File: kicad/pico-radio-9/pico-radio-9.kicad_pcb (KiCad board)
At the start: 2 copper layers, 115.8 x 67.5 mm, 58 parts, among them J1 FM antenna, J2 SW antenna, J3 MW/SW antenna kapcsoló, J4 HF Amplifier, J5 Batterry, Q1 PN2222A, Q2 PN2222A, Q3 PN2222A, SW1 Reset, U1 SI4732-A10-GS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

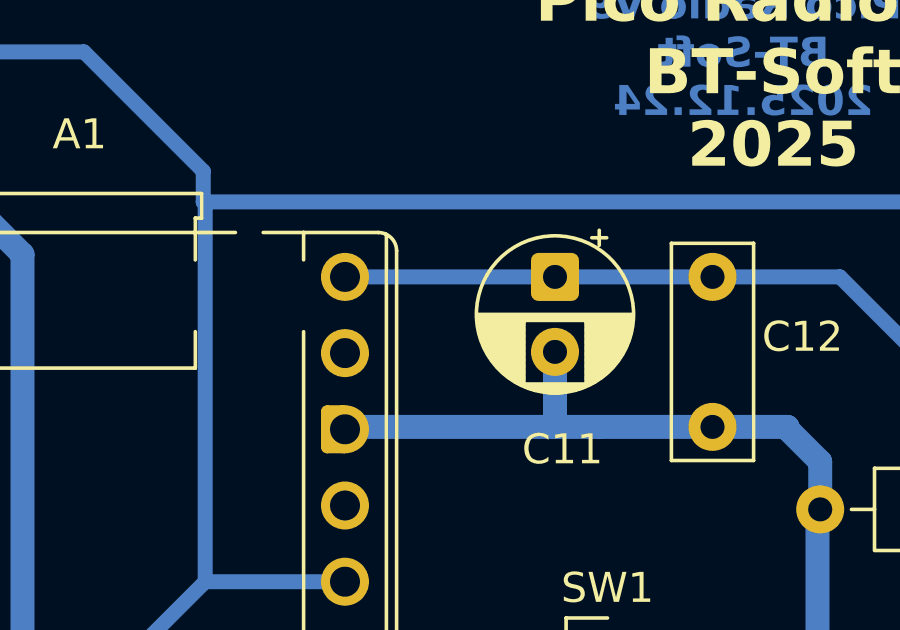
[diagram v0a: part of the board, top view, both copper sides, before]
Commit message: Vsys - Vbus power modification
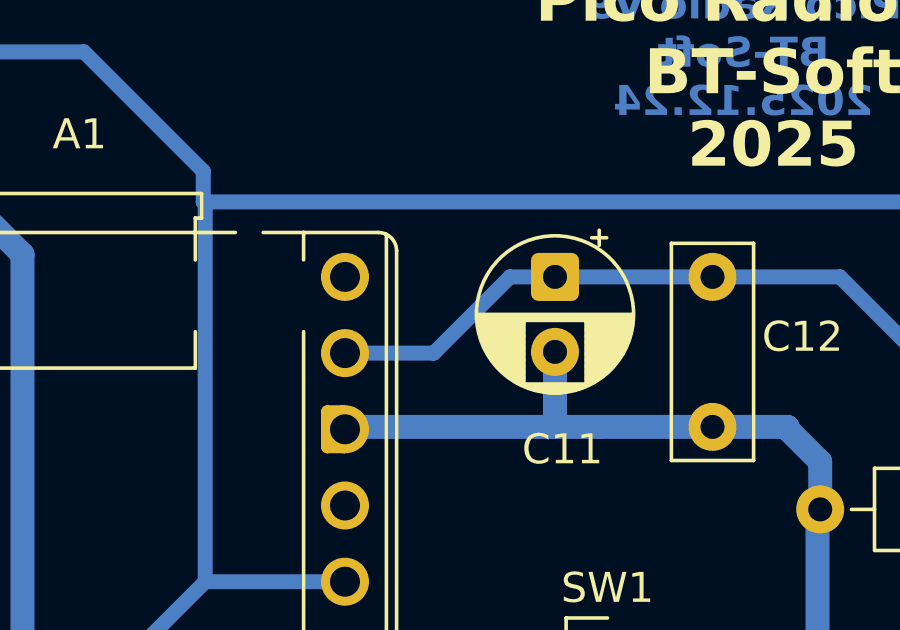
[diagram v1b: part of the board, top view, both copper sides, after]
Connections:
- A1 pad 40: +Vbus -> unconnected-(A1-VBUS-Pad40)
- BZ1 pad 1: +Vbus -> +Vsys
- C11 pad 1: +Vbus -> +Vsys
- C12 pad 1: +Vbus -> +Vsys
- JP4 pad 2: +Vbus -> +Vsys
- R12 pad 1: +Vbus -> +Vsys
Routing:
- net +Vsys: track 0.00 -> 59.6 mm
- net +Vbus: track 58.5 -> 0.00 mm
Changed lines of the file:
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@@
 	(net 16 "BUZZER")
 	(net 17 "/RST")
-	(net 18 "+Vbus")
+	(net 18 "unconnected-(A1-VBUS-Pad40)")
 	(net 19 "/SDI")
 	(net 20 "unconnected-(A1-GPIO23-Pad26)")
@@
 			(layers "*.Cu" "*.Mask")
 			(remove_unused_layers no)
-			(net 18 "+Vbus")
+			(net 4 "+Vsys")
 			(pinfunction "+")
 			(pintype "passive")
@@
 			(layers "*.Cu" "*.Mask")
 			(remove_unused_layers no)
-			(net 18 "+Vbus")
+			(net 18 "unconnected-(A1-VBUS-Pad40)")
 			(pinfunction "VBUS")
-			(pintype "power_out")
+			(pintype "power_out+no_connect")
 		)
 		(group ""
@@
 			(remove_unused_layers no)
 			(roundrect_rratio 0.15625)
-			(net 18 "+Vbus")
+			(net 4 "+Vsys")
 			(pintype "passive")
 		)
@@
 			(layers "*.Cu" "*.Mask")
 			(remove_unused_layers no)
-			(net 18 "+Vbus")
+			(net 4 "+Vsys")
 			(pintype "passive")
 		)
@@
 			(layers "*.Cu" "*.Mask")
 			(remove_unused_layers no)
-			(net 18 "+Vbus")
+			(net 4 "+Vsys")
 			(pinfunction "B")
 			(pintype "passive")
@@
 			(layers "*.Cu" "*.Mask")
 			(remove_unused_layers no)
-			(net 18 "+Vbus")
+			(net 4 "+Vsys")
 			(pintype "passive")
 		)
@@
 	)
 	(segment
+		(start 132.025 77.065)
+		(end 131.975 77.115)
+		(width 0.2)
+		(layer "B.Cu")
+		(net 4)
+	)
+	(segment
+		(start 132.025 69.275)
+		(end 132.025 77.065)
+		(width 0.5)
+		(layer "B.Cu")
+		(net 4)
+	)
+	(segment
+		(start 118.225 38.525)
+		(end 116.725 38.525)
+		(width 0.5)
+		(layer "B.Cu")
+		(net 4)
+	)
+	(segment
+		(start 116.725 38.525)
+		(end 114.185 41.065)
+		(width 0.5)
+		(layer "B.Cu")
+		(net 4)
+	)
+	(segment
+		(start 123.475 38.525)
+		(end 127.725 38.525)
+		(width 0.5)
+		(layer "B.Cu")
+		(net 4)
+	)
+	(segment
+		(start 131.725 51.195)
+		(end 131.725 55.525)
+		(width 0.5)
+		(layer "B.Cu")
+		(net 4)
+	)
+	(segment
+		(start 134.475 58.275)
+		(end 134.475 64.025)
+		(width 0.5)
+		(layer "B.Cu")
+		(net 4)
+	)
+	(segment
+		(start 118.225 38.525)
+		(end 123.475 38.525)
+		(width 0.5)
+		(layer "B.Cu")
+		(net 4)
+	)
+	(segment
+		(start 131.975 69.325)
+		(end 132.025 69.275)
+		(width 0.2)
+		(layer "B.Cu")
+		(net 4)
+	)
+	(segment
+		(start 132.025 66.475)
+		(end 132.025 68.724)
+		(width 0.5)
+		(layer "B.Cu")
+		(net 4)
+	)
+	(segment
+		(start 131.725 55.525)
+		(end 134.475 58.275)
+		(width 0.5)
+		(layer "B.Cu")
+		(net 4)
+	)
+	(segment
+		(start 114.185 41.065)
+		(end 111.225 41.065)
+		(width 0.5)
+		(layer "B.Cu")
+		(net 4)
+	)
+	(segment
+		(start 134.475 64.025)
+		(end 132.025 66.475)
+		(width 0.5)
+		(layer "B.Cu")
+		(net 4)
+	)
+	(segment
+		(start 131.725 42.525)
+		(end 131.725 51.195)
+		(width 0.5)
+		(layer "B.Cu")
+		(net 4)
+	)
+	(segment
+		(start 131.975 69.876)
+		(end 132.025 69.826)
+		(width 0.2)
+		(layer "B.Cu")
+		(net 4)
+	)
+	(segment
+		(start 127.725 38.525)
+		(end 131.725 42.525)
+		(width 0.5)
+		(layer "B.Cu")
+		(net 4)
+	)
+	(segment
 		(start 93.445 56.305)
 		(end 95.445 56.305)
@@
 	)
 	(segment
-		(start 132.025 77.065)
-		(end 131.975 77.115)
-		(width 0.2)
-		(layer "B.Cu")
-		(net 18)
-	)
-	(segment
-		(start 132.025 69.275)
-		(end 132.025 77.065)
-		(width 0.5)
-		(layer "B.Cu")
-		(net 18)
-	)
-	(segment
-		(start 123.475 38.525)
-		(end 127.725 38.525)
-		(width 0.5)
-		(layer "B.Cu")
-		(net 18)
-	)
-	(segment
-		(start 118.225 38.525)
-		(end 111.225 38.525)
-		(width 0.5)
-		(layer "B.Cu")
-		(net 18)
-	)
-	(segment
-		(start 131.725 51.195)
-		(end 131.725 55.525)
-		(width 0.5)
-		(layer "B.Cu")
-		(net 18)
-	)
-	(segment
-		(start 134.475 58.275)
-		(end 134.475 64.025)
-		(width 0.5)
-		(layer "B.Cu")
-		(net 18)
-	)
-	(segment
-		(start 118.225 38.525)
-		(end 123.475 38.525)
-		(width 0.5)
-		(layer "B.Cu")
-		(net 18)
-	)
-	(segment
-		(start 131.975 69.325)
-		(end 132.025 69.275)
-		(width 0.2)
-		(layer "B.Cu")
-		(net 18)
-	)
-	(segment
-		(start 132.025 66.475)
-		(end 132.025 68.724)
-		(width 0.5)
-		(layer "B.Cu")
-		(net 18)
-	)
-	(segment
-		(start 131.725 55.525)
-		(end 134.475 58.275)
-		(width 0.5)
-		(layer "B.Cu")
-		(net 18)
-	)
-	(segment
-		(start 134.475 64.025)
-		(end 132.025 66.475)
-		(width 0.5)
-		(layer "B.Cu")
-		(net 18)
-	)
-	(segment
-		(start 131.725 42.525)
-		(end 131.725 51.195)
-		(width 0.5)
-		(layer "B.Cu")
-		(net 18)
-	)
-	(segment
-		(start 131.975 69.876)
-		(end 132.025 69.826)
-		(width 0.2)
-		(layer "B.Cu")
-		(net 18)
-	)
-	(segment
-		(start 127.725 38.525)
-		(end 131.725 42.525)
-		(width 0.5)
-		(layer "B.Cu")
-		(net 18)
-	)
-	(segment

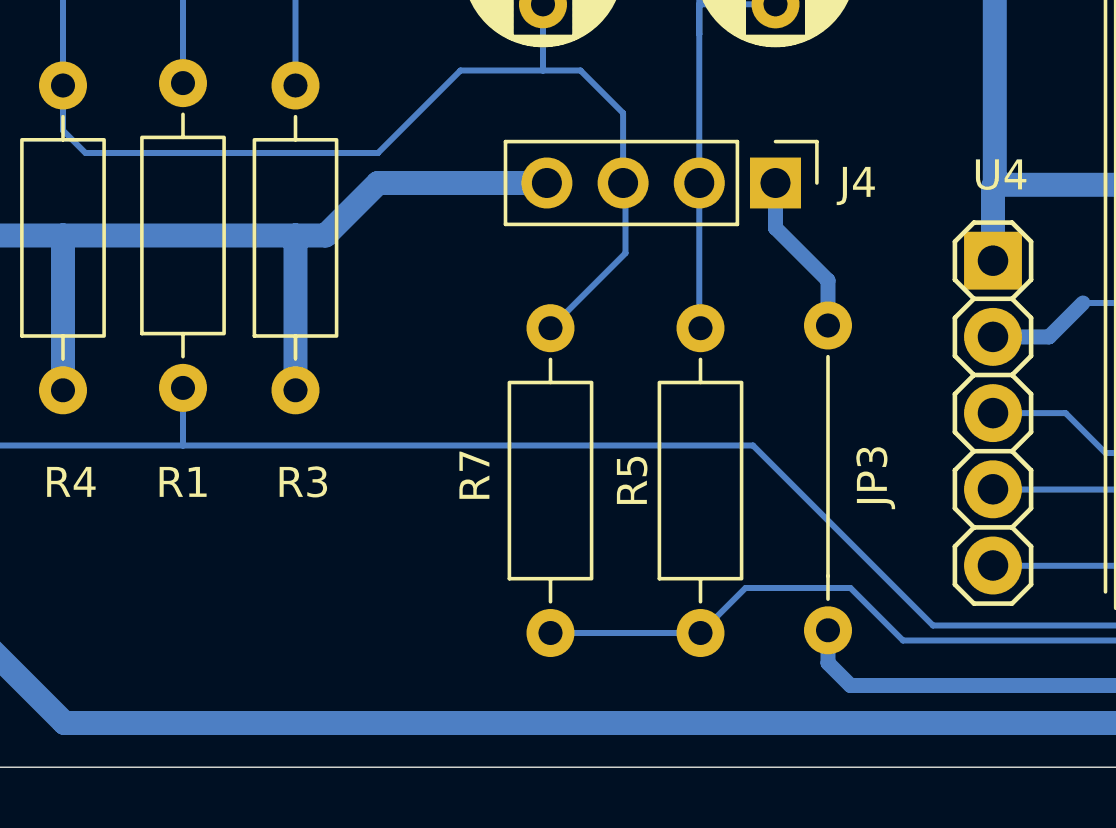
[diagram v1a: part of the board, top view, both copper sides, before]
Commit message: Add capacitors C13 and C14 to the schematic and update connections
- Added capacitor C13 (100nF) at coordinates (96.52, 148.59) with appropriate properties.
- Added capacitor C14 (100nF) at coordinates (96.52, 171.45) with appropriate properties.
- Updated wire connections for C13 and C14.
- Changed the value of resistor R1 from 100k to 47k.
- Adjusted the position of capacitor C7 for better layout.
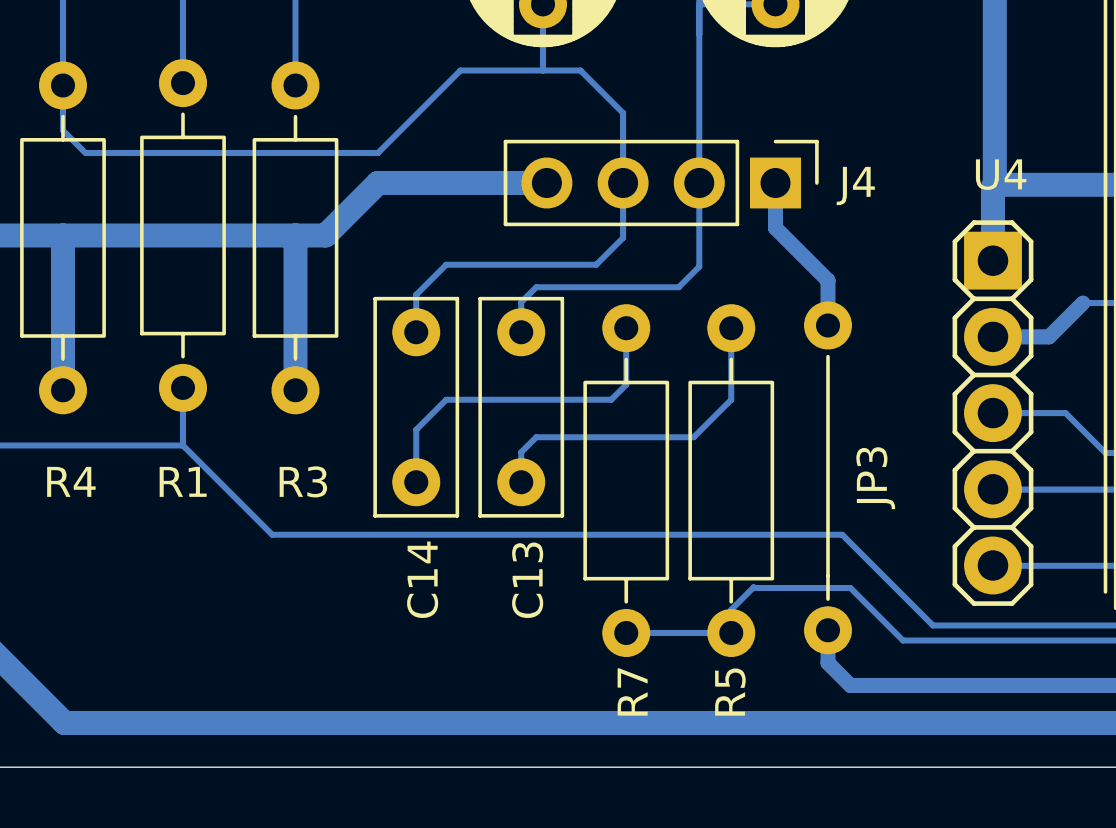
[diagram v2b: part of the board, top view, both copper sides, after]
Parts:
- added C13: 100nF, Capacitor_THT:C_Disc_D7.0mm_W2.5mm_P5.00mm, F.Cu at (72.2, 84.0)
- added C14: 100nF, Capacitor_THT:C_Disc_D7.0mm_W2.5mm_P5.00mm, F.Cu at (68.8, 84.0)
- R11: value 100k -> 47k
- moved R7 2.53 mm to (75.8, 89.0)
- moved R5 1.03 mm to (79.2, 89.0)
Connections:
- R5 pad 2: AUDIO_R -> Net-(C13-Pad1)
- R7 pad 2: AUDIO_L -> Net-(C14-Pad1)
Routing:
- net Net-(C14-Pad1): track 0.00 -> 11.3 mm
- net Net-(C13-Pad1): track 0.00 -> 11.1 mm
- net AUDIO_R: track 32.6 -> 37.9 mm
- net AUDIO_L: track 36.6 -> 41.5 mm
- net Net-(U3B--): track 108.1 -> 106.1 mm
